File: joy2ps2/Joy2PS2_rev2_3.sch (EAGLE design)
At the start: 7 parts

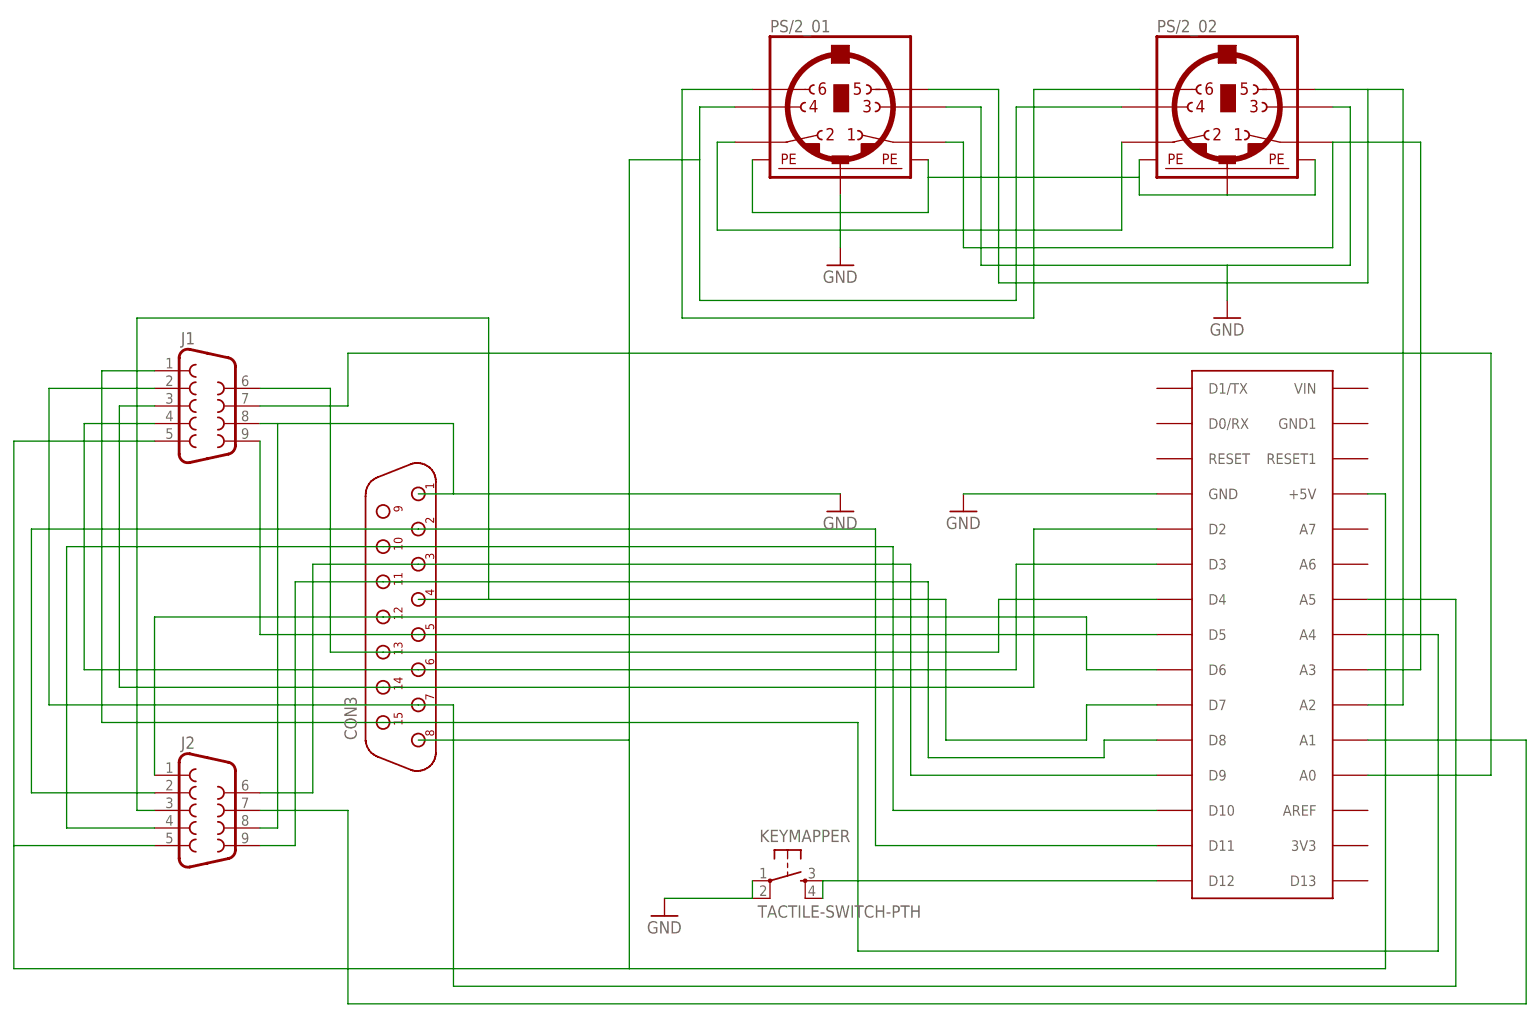
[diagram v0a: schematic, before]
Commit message: Mejoras visuales
Mejora visual del esquema y corrección del fichero .BRD corrupto.
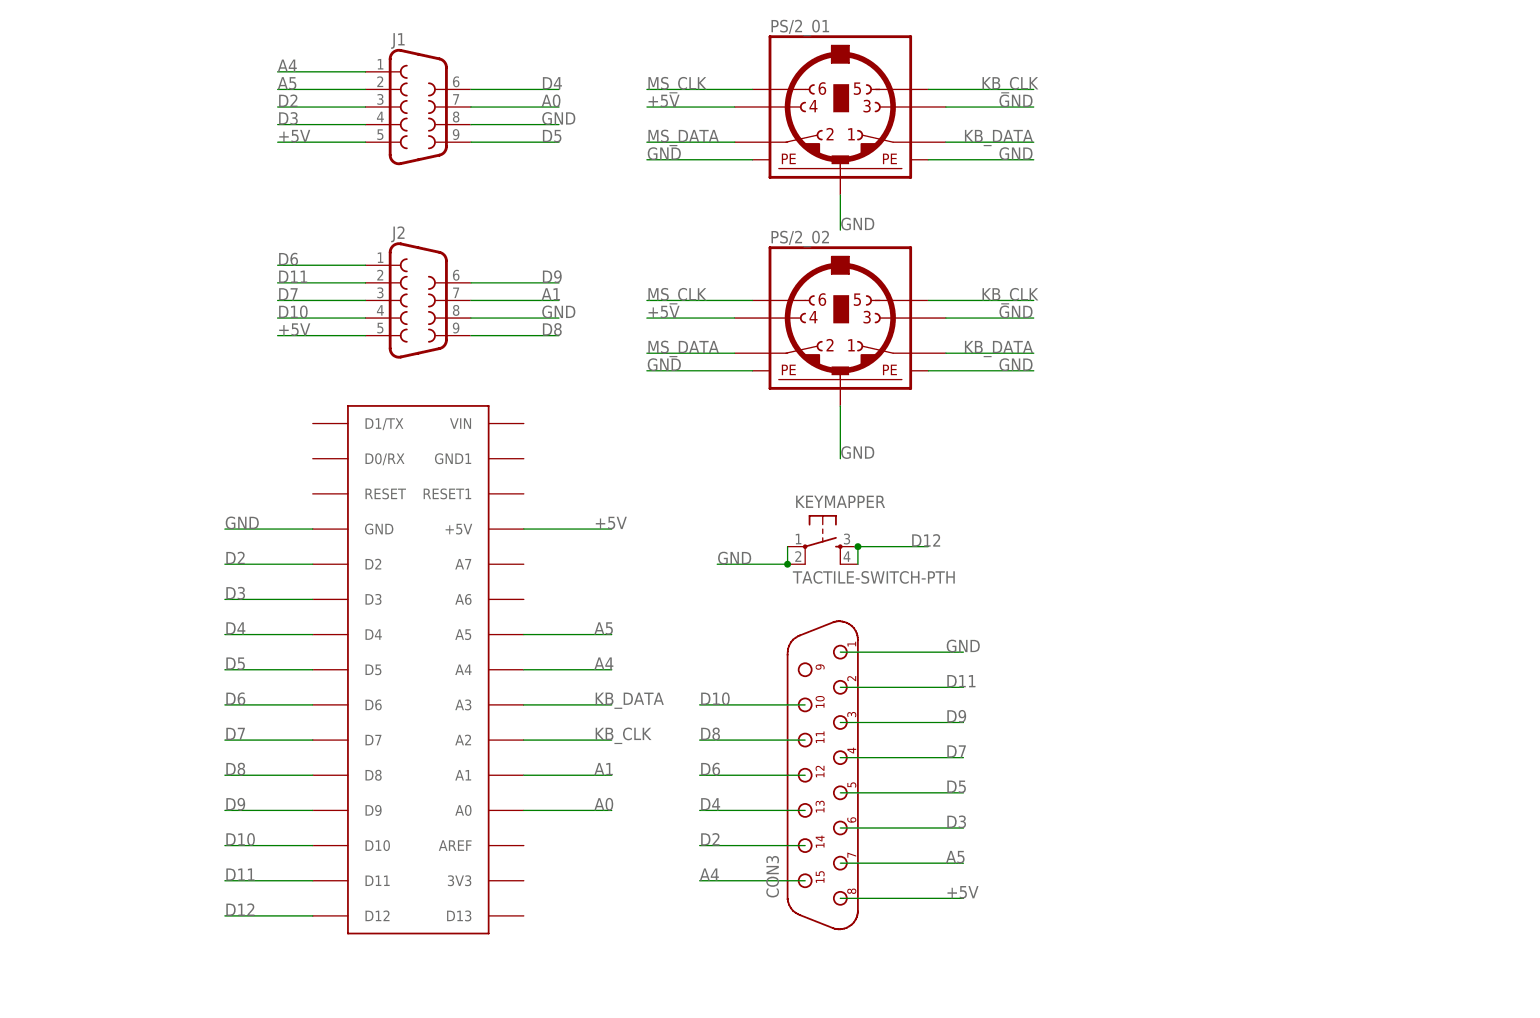
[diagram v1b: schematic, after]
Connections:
- net N$1 renamed KB_DATA
- net N$10 renamed D2
- net N$11 renamed D3
- net N$12 renamed D4
- net N$13 renamed D5
- net N$14 renamed D6
- net N$15 renamed D7
- net N$16 renamed D9
- net N$17 renamed D11
- net N$18 renamed A4
- net N$19 renamed D12
- net N$2 renamed MS_DATA
- net N$20 renamed MS_CLK
- net N$3 renamed +5V
- net N$4 renamed A0
- net N$5 renamed KB_CLK
- net N$6 renamed D10
- net N$7 renamed D8
- net N$8 renamed A1
- net N$9 renamed A5
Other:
- moved on the sheet: CON3, J1, J2, KEYMAPPER, PS/2_02
